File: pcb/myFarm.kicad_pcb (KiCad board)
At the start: 2 copper layers, 10 parts, among them J0 Conn_01x02, J1 LED, J2 SENSOR, J3 SW_LED, J4 RELAY, J5 POWER DRIVE, J6 JUMPER, J7 SW_LED, U1 WeMos_D1_mini, U2 MCP23017_MODULE

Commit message: update pcb
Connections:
- J6 pad 1: GNDREF -> Net-(J1-Pad1)
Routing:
- net Net-(J1-Pad1): track 123.3 -> 132.2 mm
- net GNDREF: track 156.0 -> 149.6 mm
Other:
- board outline added: 63.5 x 52.1 mm
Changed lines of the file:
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@@
-(kicad_pcb (version 20171130) (host pcbnew 5.1.2-f72e74a~84~ubuntu19.04.1)
+(kicad_pcb (version 20171130) (host pcbnew 5.1.3-ffb9f22~84~ubuntu19.04.1)
   (general
     (thickness 1.6)
-    (drawings 0)
-    (tracks 88)
+    (drawings 4)
+    (tracks 87)
     (zones 0)
     (modules 10)
@@
     (34 B.Paste user hide)
     (35 F.Paste user hide)
-    (36 B.SilkS user hide)
-    (37 F.SilkS user hide)
+    (36 B.SilkS user)
+    (37 F.SilkS user)
     (38 B.Mask user hide)
     (39 F.Mask user hide)
@@
     (42 Eco1.User user hide)
     (43 Eco2.User user hide)
-    (44 Edge.Cuts user hide)
+    (44 Edge.Cuts user)
     (45 Margin user hide)
     (46 B.CrtYd user hide)
@@
   )
   (setup
-    (last_trace_width 0.25)
+    (last_trace_width 0.5)
+    (user_trace_width 0.5)
     (user_trace_width 1)
     (user_trace_width 2)
@@
     (visible_elements FFFFFFFF)
     (pcbplotparams
-      (layerselection 0x010fc_ffffffff)
+      (layerselection 0x010f0_ffffffff)
       (usegerberextensions false)
       (usegerberattributes false)
@@
       (outputformat 1)
       (mirror false)
-      (drillshape 1)
+      (drillshape 0)
       (scaleselection 1)
-      (outputdirectory ""))
+      (outputdirectory "gerber/"))
   )
   (net 0 "")
@@
       (net 19 "Net-(J6-Pad2)"))
     (pad 1 thru_hole rect (at 0 0 270) (size 1.7 1.7) (drill 1) (layers *.Cu *.Mask)
-      (net 11 GNDREF))
+      (net 2 "Net-(J1-Pad1)"))
     (model ${KISYS3DMOD}/Connector_PinHeader_2.54mm.3dshapes/PinHeader_1x03_P2.54mm_Vertical.wrl
       (at (xyz 0 0 0))
@@
       (net 11 GNDREF))
   )
-  (segment (start 105.41 72.39) (end 107.95 72.39) (width 0.25) (layer B.Cu) (net 1))
-  (segment (start 94.805009 61.785009) (end 105.41 72.39) (width 0.25) (layer B.Cu) (net 1))
-  (segment (start 79.565009 61.785009) (end 94.805009 61.785009) (width 0.25) (layer B.Cu) (net 1))
-  (segment (start 78.74 57.15) (end 78.74 60.96) (width 0.25) (layer B.Cu) (net 1))
-  (segment (start 78.74 60.96) (end 79.565009 61.785009) (width 0.25) (layer B.Cu) (net 1))
+  (gr_line (start 125.73 48.26) (end 62.23 48.26) (layer Edge.Cuts) (width 0.05))
+  (gr_line (start 125.73 100.33) (end 125.73 48.26) (layer Edge.Cuts) (width 0.05))
+  (gr_line (start 62.23 100.33) (end 125.73 100.33) (layer Edge.Cuts) (width 0.05))
+  (gr_line (start 62.23 48.26) (end 62.23 100.33) (layer Edge.Cuts) (width 0.05))
+  (segment (start 105.41 72.39) (end 107.95 72.39) (width 0.5) (layer B.Cu) (net 1))
+  (segment (start 94.805009 61.785009) (end 105.41 72.39) (width 0.5) (layer B.Cu) (net 1))
+  (segment (start 79.565009 61.785009) (end 94.805009 61.785009) (width 0.5) (layer B.Cu) (net 1))
+  (segment (start 78.74 57.15) (end 78.74 60.96) (width 0.5) (layer B.Cu) (net 1))
+  (segment (start 78.74 60.96) (end 79.565009 61.785009) (width 0.5) (layer B.Cu) (net 1))
   (segment (start 68.58 89.48) (end 68.58 87.63) (width 1) (layer F.Cu) (net 2))
   (segment (start 69.27 90.17) (end 68.58 89.48) (width 1) (layer F.Cu) (net 2))
@@
   (segment (start 116.84 63.5) (end 107.95 63.5) (width 1) (layer B.Cu) (net 2))
   (segment (start 107.95 63.5) (end 101.6 63.5) (width 1) (layer B.Cu) (net 2))
-  (segment (start 90.17 57.15) (end 104.14 71.12) (width 0.25) (layer F.Cu) (net 3))
-  (segment (start 104.14 76.2) (end 107.95 80.01) (width 0.25) (layer F.Cu) (net 3))
-  (segment (start 104.14 71.12) (end 104.14 76.2) (width 0.25) (layer F.Cu) (net 3))
-  (segment (start 92.71 57.15) (end 92.71 58.42) (width 0.25) (layer F.Cu) (net 4))
-  (segment (start 92.71 58.42) (end 105.41 71.12) (width 0.25) (layer F.Cu) (net 4))
-  (segment (start 105.41 74.93) (end 107.95 77.47) (width 0.25) (layer F.Cu) (net 4))
-  (segment (start 105.41 71.12) (end 105.41 74.93) (width 0.25) (layer F.Cu) (net 4))
-  (segment (start 110.49 74.93) (end 116.84 68.58) (width 0.25) (layer B.Cu) (net 5))
-  (segment (start 110.49 72.39) (end 116.84 66.04) (width 0.25) (layer B.Cu) (net 6))
-  (segment (start 110.49 80.01) (end 116.84 80.01) (width 0.25) (layer F.Cu) (net 7))
-  (segment (start 110.49 77.47) (end 116.84 77.47) (width 0.25) (layer F.Cu) (net 8))
-  (segment (start 92.71 85.09) (end 96.52 85.09) (width 0.25) (layer F.Cu) (net 9))
-  (segment (start 96.52 85.09) (end 96.52 82.55) (width 0.25) (layer F.Cu) (net 9))
-  (segment (start 96.52 82.55) (end 99.06 82.55) (width 0.25) (layer F.Cu) (net 9))
-  (segment (start 92.71 82.55) (end 95.25 82.55) (width 0.25) (layer F.Cu) (net 10))
-  (segment (start 95.25 82.55) (end 95.25 80.01) (width 0.25) (layer F.Cu) (net 10))
-  (segment (start 95.25 80.01) (end 99.06 80.01) (width 0.25) (layer F.Cu) (net 10))
+  (segment (start 81.28 64.77) (end 81.28 73.66) (width 1) (layer F.Cu) (net 2))
+  (segment (start 90.17 57.15) (end 104.14 71.12) (width 0.5) (layer F.Cu) (net 3))
+  (segment (start 104.14 76.2) (end 107.95 80.01) (width 0.5) (layer F.Cu) (net 3))
+  (segment (start 104.14 71.12) (end 104.14 76.2) (width 0.5) (layer F.Cu) (net 3))
+  (segment (start 92.71 57.15) (end 92.71 58.42) (width 0.5) (layer F.Cu) (net 4))
+  (segment (start 92.71 58.42) (end 105.41 71.12) (width 0.5) (layer F.Cu) (net 4))
+  (segment (start 105.41 74.93) (end 107.95 77.47) (width 0.5) (layer F.Cu) (net 4))
+  (segment (start 105.41 71.12) (end 105.41 74.93) (width 0.5) (layer F.Cu) (net 4))
+  (segment (start 110.49 74.93) (end 116.84 68.58) (width 0.5) (layer B.Cu) (net 5))
+  (segment (start 110.49 72.39) (end 116.84 66.04) (width 0.5) (layer B.Cu) (net 6))
+  (segment (start 110.49 80.01) (end 116.84 80.01) (width 0.5) (layer F.Cu) (net 7))
+  (segment (start 110.49 77.47) (end 116.84 77.47) (width 0.5) (layer F.Cu) (net 8))
+  (segment (start 92.71 85.09) (end 96.52 85.09) (width 0.5) (layer F.Cu) (net 9))
+  (segment (start 96.52 85.09) (end 96.52 82.55) (width 0.5) (layer F.Cu) (net 9))
+  (segment (start 96.52 82.55) (end 99.06 82.55) (width 0.5) (layer F.Cu) (net 9))
+  (segment (start 92.71 82.55) (end 95.25 82.55) (width 0.5) (layer F.Cu) (net 10))
+  (segment (start 95.25 82.55) (end 95.25 80.01) (width 0.5) (layer F.Cu) (net 10))
+  (segment (start 95.25 80.01) (end 99.06 80.01) (width 0.5) (layer F.Cu) (net 10))
   (segment (start 110.49 60.96) (end 107.95 58.42) (width 2) (layer F.Cu) (net 11))
   (segment (start 110.49 67.31) (end 110.49 60.96) (width 2) (layer F.Cu) (net 11))
@@
   (segment (start 68.58 82.55) (end 68.58 58.42) (width 2) (layer F.Cu) (net 11))
   (segment (start 68.58 58.42) (end 73.66 53.34) (width 2) (layer F.Cu) (net 11))
-  (segment (start 81.28 64.77) (end 84.13 64.77) (width 2) (layer F.Cu) (net 11))
   (segment (start 87.63 57.15) (end 87.63 64.77) (width 2) (layer F.Cu) (net 11))
-  (segment (start 84.13 64.77) (end 87.63 64.77) (width 2) (layer F.Cu) (net 11))
   (segment (start 87.63 64.77) (end 87.63 83.62763) (width 2) (layer F.Cu) (net 11))
   (segment (start 92.71 72.39) (end 99.06 72.39) (width 1) (layer F.Cu) (net 11))
   (segment (start 101.6 55.88) (end 107.95 55.88) (width 2) (layer F.Cu) (net 12))
   (segment (start 68.58 85.09) (end 69.85 85.09) (width 0.25) (layer F.Cu) (net 13))
-  (segment (start 72.39 82.55) (end 76.2 82.55) (width 0.25) (layer F.Cu) (net 13))
-  (segment (start 69.85 85.09) (end 72.39 82.55) (width 0.25) (layer F.Cu) (net 13))
-  (segment (start 110.49 90.17) (end 116.84 90.17) (width 0.25) (layer F.Cu) (net 14))
-  (segment (start 110.49 87.63) (end 116.84 87.63) (width 0.25) (layer F.Cu) (net 15))
-  (segment (start 110.49 85.09) (end 116.84 85.09) (width 0.25) (layer F.Cu) (net 16))
-  (segment (start 110.49 82.55) (end 116.84 82.55) (width 0.25) (layer F.Cu) (net 17))
-  (segment (start 76.2 64.77) (end 72.39 68.58) (width 0.25) (layer B.Cu) (net 18))
-  (segment (start 72.39 68.58) (end 72.39 92.71) (width 0.25) (layer B.Cu) (net 18))
-  (segment (start 72.39 92.71) (end 95.25 92.71) (width 0.25) (layer B.Cu) (net 18))
+  (segment (start 72.39 82.55) (end 76.2 82.55) (width 0.5) (layer F.Cu) (net 13))
+  (segment (start 69.85 85.09) (end 72.39 82.55) (width 0.5) (layer F.Cu) (net 13))
+  (segment (start 110.49 90.17) (end 116.84 90.17) (width 0.5) (layer F.Cu) (net 14))
+  (segment (start 110.49 87.63) (end 116.84 87.63) (width 0.5) (layer F.Cu) (net 15))
+  (segment (start 110.49 85.09) (end 116.84 85.09) (width 0.5) (layer F.Cu) (net 16))
+  (segment (start 110.49 82.55) (end 116.84 82.55) (width 0.5) (layer F.Cu) (net 17))
+  (segment (start 76.2 64.77) (end 72.39 68.58) (width 0.5) (layer B.Cu) (net 18))
+  (segment (start 72.39 68.58) (end 72.39 92.71) (width 0.5) (layer B.Cu) (net 18))
+  (segment (start 72.39 92.71) (end 95.25 92.71) (width 0.5) (layer B.Cu) (net 18))
   (segment (start 98.86 77.47) (end 99.06 77.47) (width 0.25) (layer B.Cu) (net 18))
-  (segment (start 95.25 81.08) (end 98.86 77.47) (width 0.25) (layer B.Cu) (net 18))
-  (segment (start 95.25 92.71) (end 95.25 81.08) (width 0.25) (layer B.Cu) (net 18))
-  (segment (start 92.71 74.93) (end 85.09 74.93) (width 0.25) (layer B.Cu) (net 19))
-  (segment (start 85.09 74.93) (end 78.74 68.58) (width 0.25) (layer B.Cu) (net 19))
-  (segment (start 78.74 68.58) (end 78.74 64.77) (width 0.25) (layer B.Cu) (net 19))
+  (segment (start 95.25 81.08) (end 98.86 77.47) (width 0.5) (layer B.Cu) (net 18))
+  (segment (start 95.25 92.71) (end 95.25 81.08) (width 0.5) (layer B.Cu) (net 18))
+  (segment (start 92.71 74.93) (end 85.09 74.93) (width 0.5) (layer B.Cu) (net 19))
+  (segment (start 85.09 74.93) (end 78.74 68.58) (width 0.5) (layer B.Cu) (net 19))
+  (segment (start 78.74 68.58) (end 78.74 64.77) (width 0.5) (layer B.Cu) (net 19))
   (zone (net 11) (net_name GNDREF) (layer B.Cu) (hatch edge 0.508)
     (connect_pads (clearance 0.508))

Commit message: update pcb
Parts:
- moved J7 6.84 mm to (108.0, 58.4), turned to 270 degrees
- moved J2 5.08 mm to (68.6, 82.5)
- moved J0 4.58 mm to (110.5, 52.1)
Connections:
- U1 pad 3: Net-(J2-Pad2) -> (no net)
- U1 pad 4: (no net) -> Net-(J2-Pad2)
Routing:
- net Net-(J1-Pad1): track 132.2 -> 141.2 mm
- net Net-(J0-Pad1): track 6.35 -> 8.89 mm
- net GNDREF: track 149.6 -> 148.3 mm
- removed copper zone on B.Cu, net GNDREF
- removed copper zone on F.Cu, net GNDREF

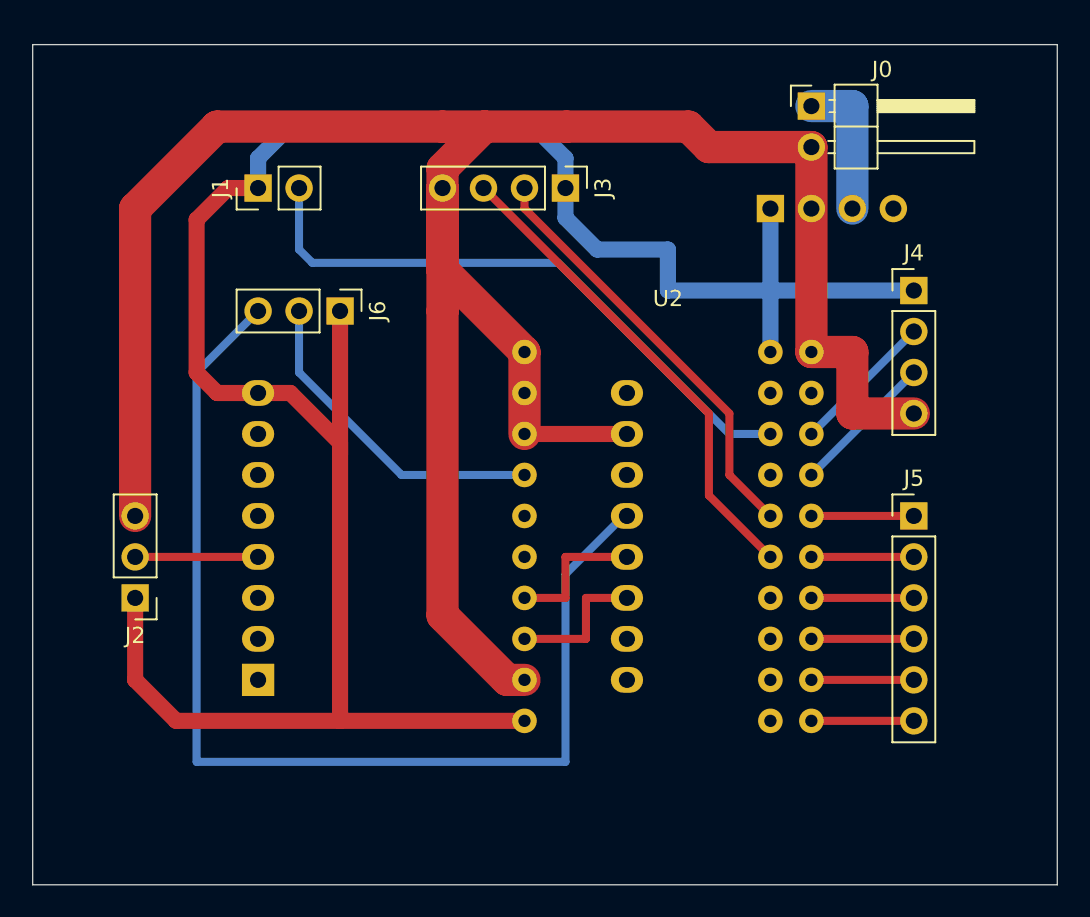
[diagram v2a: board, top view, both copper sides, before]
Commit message: swap connect j3
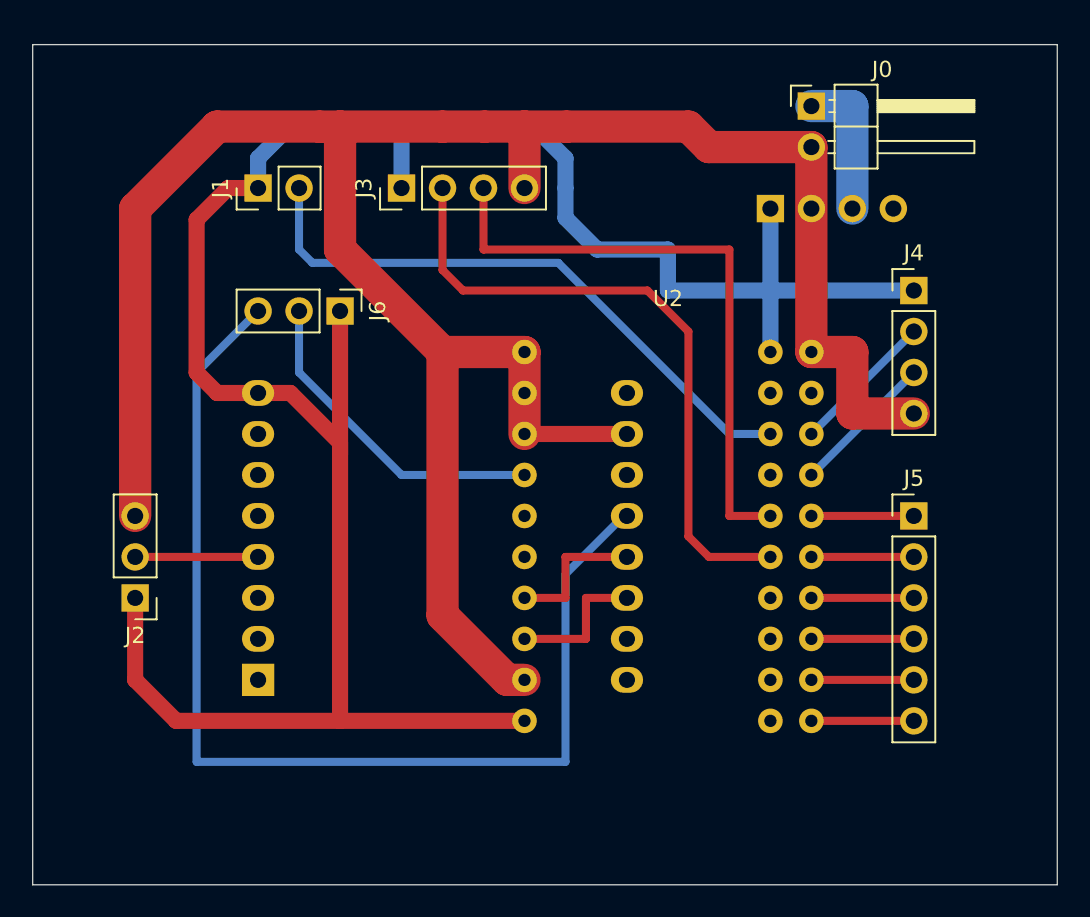
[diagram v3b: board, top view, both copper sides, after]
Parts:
- moved J3 10.2 mm to (85.1, 57.1), turned to 90 degrees
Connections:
- U2 pad 3: Net-(J3-Pad2) -> Net-(J3-Pad3)
- U2 pad 4: Net-(J3-Pad3) -> Net-(J3-Pad2)
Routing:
- net Net-(J3-Pad2): track 26.6 -> 40.2 mm
- net Net-(J3-Pad3): track 30.2 -> 38.1 mm
- net Net-(J1-Pad1): track 141.2 -> 145.0 mm
- net GNDREF: track 148.3 -> 146.4 mm
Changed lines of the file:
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@@
     (thickness 1.6)
     (drawings 4)
-    (tracks 87)
+    (tracks 95)
     (zones 0)
     (modules 10)
@@
   )
   (setup
-    (last_trace_width 2)
+    (last_trace_width 0.5)
     (user_trace_width 0.5)
     (user_trace_width 1)
@@
   )
   (module Connector_PinHeader_2.54mm:PinHeader_1x04_P2.54mm_Vertical (layer F.Cu)
-    (at 95.25 57.15 270)
+    (at 85.09 57.15 90)
     (descr "Through hole straight pin header, 1x04, 2.54mm pitch, single row")
     (tags "Through hole pin header THT 1x04 2.54mm single row")
@@
     (fp_line (start 1.27 -1.27) (end 1.27 8.89) (layer F.Fab) (width 0.1))
     (fp_line (start -0.635 -1.27) (end 1.27 -1.27) (layer F.Fab) (width 0.1))
-    (pad 4 thru_hole oval (at 0 7.62 270) (size 1.7 1.7) (drill 1) (layers *.Cu *.Mask)
-      (net 11 GNDREF))
-    (pad 3 thru_hole oval (at 0 5.08 270) (size 1.7 1.7) (drill 1) (layers *.Cu *.Mask)
+    (pad 4 thru_hole oval (at 0 7.62 90) (size 1.7 1.7) (drill 1) (layers *.Cu *.Mask)
+      (net 11 GNDREF))
+    (pad 3 thru_hole oval (at 0 5.08 90) (size 1.7 1.7) (drill 1) (layers *.Cu *.Mask)
       (net 3 "Net-(J3-Pad3)"))
-    (pad 2 thru_hole oval (at 0 2.54 270) (size 1.7 1.7) (drill 1) (layers *.Cu *.Mask)
+    (pad 2 thru_hole oval (at 0 2.54 90) (size 1.7 1.7) (drill 1) (layers *.Cu *.Mask)
       (net 4 "Net-(J3-Pad2)"))
-    (pad 1 thru_hole rect (at 0 0 270) (size 1.7 1.7) (drill 1) (layers *.Cu *.Mask)
+    (pad 1 thru_hole rect (at 0 0 90) (size 1.7 1.7) (drill 1) (layers *.Cu *.Mask)
       (net 2 "Net-(J1-Pad1)"))
     (model ${KISYS3DMOD}/Connector_PinHeader_2.54mm.3dshapes/PinHeader_1x04_P2.54mm_Vertical.wrl
@@
       (net 14 "Net-(J5-Pad6)"))
     (pad 4 thru_hole circle (at 6.35 16.51) (size 1.524 1.524) (drill 0.762) (layers *.Cu *.Mask)
-      (net 3 "Net-(J3-Pad3)"))
+      (net 4 "Net-(J3-Pad2)"))
     (pad 8 thru_hole circle (at 6.35 26.67) (size 1.524 1.524) (drill 0.762) (layers *.Cu *.Mask))
     (pad 6 thru_hole circle (at 6.35 21.59) (size 1.524 1.524) (drill 0.762) (layers *.Cu *.Mask))
@@
     (pad 2 thru_hole circle (at 6.35 11.43) (size 1.524 1.524) (drill 0.762) (layers *.Cu *.Mask))
     (pad 3 thru_hole circle (at 6.35 13.97) (size 1.524 1.524) (drill 0.762) (layers *.Cu *.Mask)
-      (net 4 "Net-(J3-Pad2)"))
+      (net 3 "Net-(J3-Pad3)"))
     (pad 1 thru_hole circle (at 6.35 8.89) (size 1.524 1.524) (drill 0.762) (layers *.Cu *.Mask)
       (net 1 "Net-(J1-Pad2)"))
@@
   (segment (start 76.2 55.3) (end 76.2 57.15) (width 1) (layer B.Cu) (net 2))
   (segment (start 78.16 53.34) (end 76.2 55.3) (width 1) (layer B.Cu) (net 2))
-  (segment (start 93.29 53.34) (end 78.16 53.34) (width 1) (layer B.Cu) (net 2))
   (segment (start 107.95 67.31) (end 107.95 63.5) (width 1) (layer B.Cu) (net 2))
   (segment (start 116.84 63.5) (end 107.95 63.5) (width 1) (layer B.Cu) (net 2))
@@
   (segment (start 107.95 63.5) (end 101.6 63.5) (width 1) (layer B.Cu) (net 2))
   (segment (start 107.95 58.42) (end 107.95 63.5) (width 1) (layer B.Cu) (net 2))
-  (segment (start 90.17 57.15) (end 104.14 71.12) (width 0.5) (layer F.Cu) (net 3))
-  (segment (start 104.14 76.2) (end 107.95 80.01) (width 0.5) (layer F.Cu) (net 3))
-  (segment (start 104.14 71.12) (end 104.14 76.2) (width 0.5) (layer F.Cu) (net 3))
-  (segment (start 92.71 57.15) (end 92.71 58.42) (width 0.5) (layer F.Cu) (net 4))
-  (segment (start 92.71 58.42) (end 105.41 71.12) (width 0.5) (layer F.Cu) (net 4))
-  (segment (start 105.41 74.93) (end 107.95 77.47) (width 0.5) (layer F.Cu) (net 4))
-  (segment (start 105.41 71.12) (end 105.41 74.93) (width 0.5) (layer F.Cu) (net 4))
+  (segment (start 85.09 57.15) (end 85.09 53.34) (width 1) (layer B.Cu) (net 2))
+  (segment (start 93.29 53.34) (end 85.09 53.34) (width 1) (layer B.Cu) (net 2))
+  (segment (start 85.09 53.34) (end 78.16 53.34) (width 1) (layer B.Cu) (net 2))
+  (segment (start 105.41 77.47) (end 107.95 77.47) (width 0.5) (layer F.Cu) (net 3))
+  (segment (start 105.41 60.96) (end 105.41 77.47) (width 0.5) (layer F.Cu) (net 3))
+  (segment (start 90.17 57.15) (end 90.17 60.96) (width 0.5) (layer F.Cu) (net 3))
+  (segment (start 90.17 60.96) (end 105.41 60.96) (width 0.5) (layer F.Cu) (net 3))
+  (segment (start 104.14 80.01) (end 107.95 80.01) (width 0.5) (layer F.Cu) (net 4))
+  (segment (start 87.63 57.15) (end 87.63 62.23) (width 0.5) (layer F.Cu) (net 4))
+  (segment (start 102.87 78.74) (end 104.14 80.01) (width 0.5) (layer F.Cu) (net 4))
+  (segment (start 88.9 63.5) (end 100.33 63.5) (width 0.5) (layer F.Cu) (net 4))
+  (segment (start 87.63 62.23) (end 88.9 63.5) (width 0.5) (layer F.Cu) (net 4))
+  (segment (start 102.87 66.04) (end 102.87 78.74) (width 0.5) (layer F.Cu) (net 4))
+  (segment (start 100.33 63.5) (end 102.87 66.04) (width 0.5) (layer F.Cu) (net 4))
   (segment (start 110.49 74.93) (end 116.84 68.58) (width 0.5) (layer B.Cu) (net 5))
   (segment (start 110.49 72.39) (end 116.84 66.04) (width 0.5) (layer B.Cu) (net 6))
@@
   (segment (start 113.03 67.31) (end 113.03 71.12) (width 2) (layer F.Cu) (net 11))
   (segment (start 113.03 71.12) (end 116.84 71.12) (width 2) (layer F.Cu) (net 11))
-  (segment (start 87.63 55.947919) (end 87.63 57.15) (width 2) (layer F.Cu) (net 11))
-  (segment (start 90.237919 53.34) (end 87.63 55.947919) (width 2) (layer F.Cu) (net 11))
-  (segment (start 95.317919 53.34) (end 90.237919 53.34) (width 2) (layer F.Cu) (net 11))
-  (segment (start 87.63 62.23) (end 92.71 67.31) (width 2) (layer F.Cu) (net 11))
-  (segment (start 87.63 57.15) (end 87.63 62.23) (width 2) (layer F.Cu) (net 11))
   (segment (start 92.71 67.31) (end 92.71 72.39) (width 2) (layer F.Cu) (net 11))
-  (segment (start 91.63237 87.63) (end 92.71 87.63) (width 2) (layer F.Cu) (net 11))
-  (segment (start 87.63 83.62763) (end 91.63237 87.63) (width 2) (layer F.Cu) (net 11))
-  (segment (start 73.66 53.34) (end 87.63 53.34) (width 2) (layer F.Cu) (net 11))
   (segment (start 87.63 53.34) (end 90.237919 53.34) (width 2) (layer F.Cu) (net 11))
   (segment (start 68.58 58.42) (end 73.66 53.34) (width 2) (layer F.Cu) (net 11))
-  (segment (start 87.63 57.15) (end 87.63 64.77) (width 2) (layer F.Cu) (net 11))
-  (segment (start 87.63 64.77) (end 87.63 83.62763) (width 2) (layer F.Cu) (net 11))
   (segment (start 92.71 72.39) (end 99.06 72.39) (width 1) (layer F.Cu) (net 11))
   (segment (start 68.58 77.47) (end 68.58 58.42) (width 2) (layer F.Cu) (net 11))
@@
   (segment (start 102.87 53.34) (end 95.317919 53.34) (width 2) (layer F.Cu) (net 11))
   (segment (start 104.14 54.61) (end 102.87 53.34) (width 2) (layer F.Cu) (net 11))
+  (segment (start 92.71 57.15) (end 92.71 53.34) (width 2) (layer F.Cu) (net 11))
+  (segment (start 95.317919 53.34) (end 92.71 53.34) (width 2) (layer F.Cu) (net 11))
+  (segment (start 92.71 53.34) (end 90.237919 53.34) (width 2) (layer F.Cu) (net 11))
+  (segment (start 73.66 53.34) (end 80.01 53.34) (width 2) (layer F.Cu) (net 11))
+  (segment (start 81.28 60.96) (end 81.28 53.34) (width 2) (layer F.Cu) (net 11))
+  (segment (start 81.28 53.34) (end 87.63 53.34) (width 2) (layer F.Cu) (net 11))
+  (segment (start 92.71 87.63) (end 91.63237 87.63) (width 2) (layer F.Cu) (net 11))
+  (segment (start 80.01 53.34) (end 81.28 53.34) (width 2) (layer F.Cu) (net 11))
+  (segment (start 91.63237 87.63) (end 87.63 83.62763) (width 2) (layer F.Cu) (net 11))
+  (segment (start 92.71 67.31) (end 87.63 67.31) (width 2) (layer F.Cu) (net 11))
+  (segment (start 87.63 83.62763) (end 87.63 67.31) (width 2) (layer F.Cu) (net 11))
+  (segment (start 81.28 60.96) (end 87.63 67.31) (width 2) (layer F.Cu) (net 11))
   (segment (start 113.03 52.07) (end 113.03 58.42) (width 2) (layer B.Cu) (net 12))
   (segment (start 110.49 52.07) (end 113.03 52.07) (width 2) (layer B.Cu) (net 12))
